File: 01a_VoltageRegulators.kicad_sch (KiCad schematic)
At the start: 34 parts, among them U5 TPS54331, U6 TPS56637RPAR, U7 TLV75733PDBV

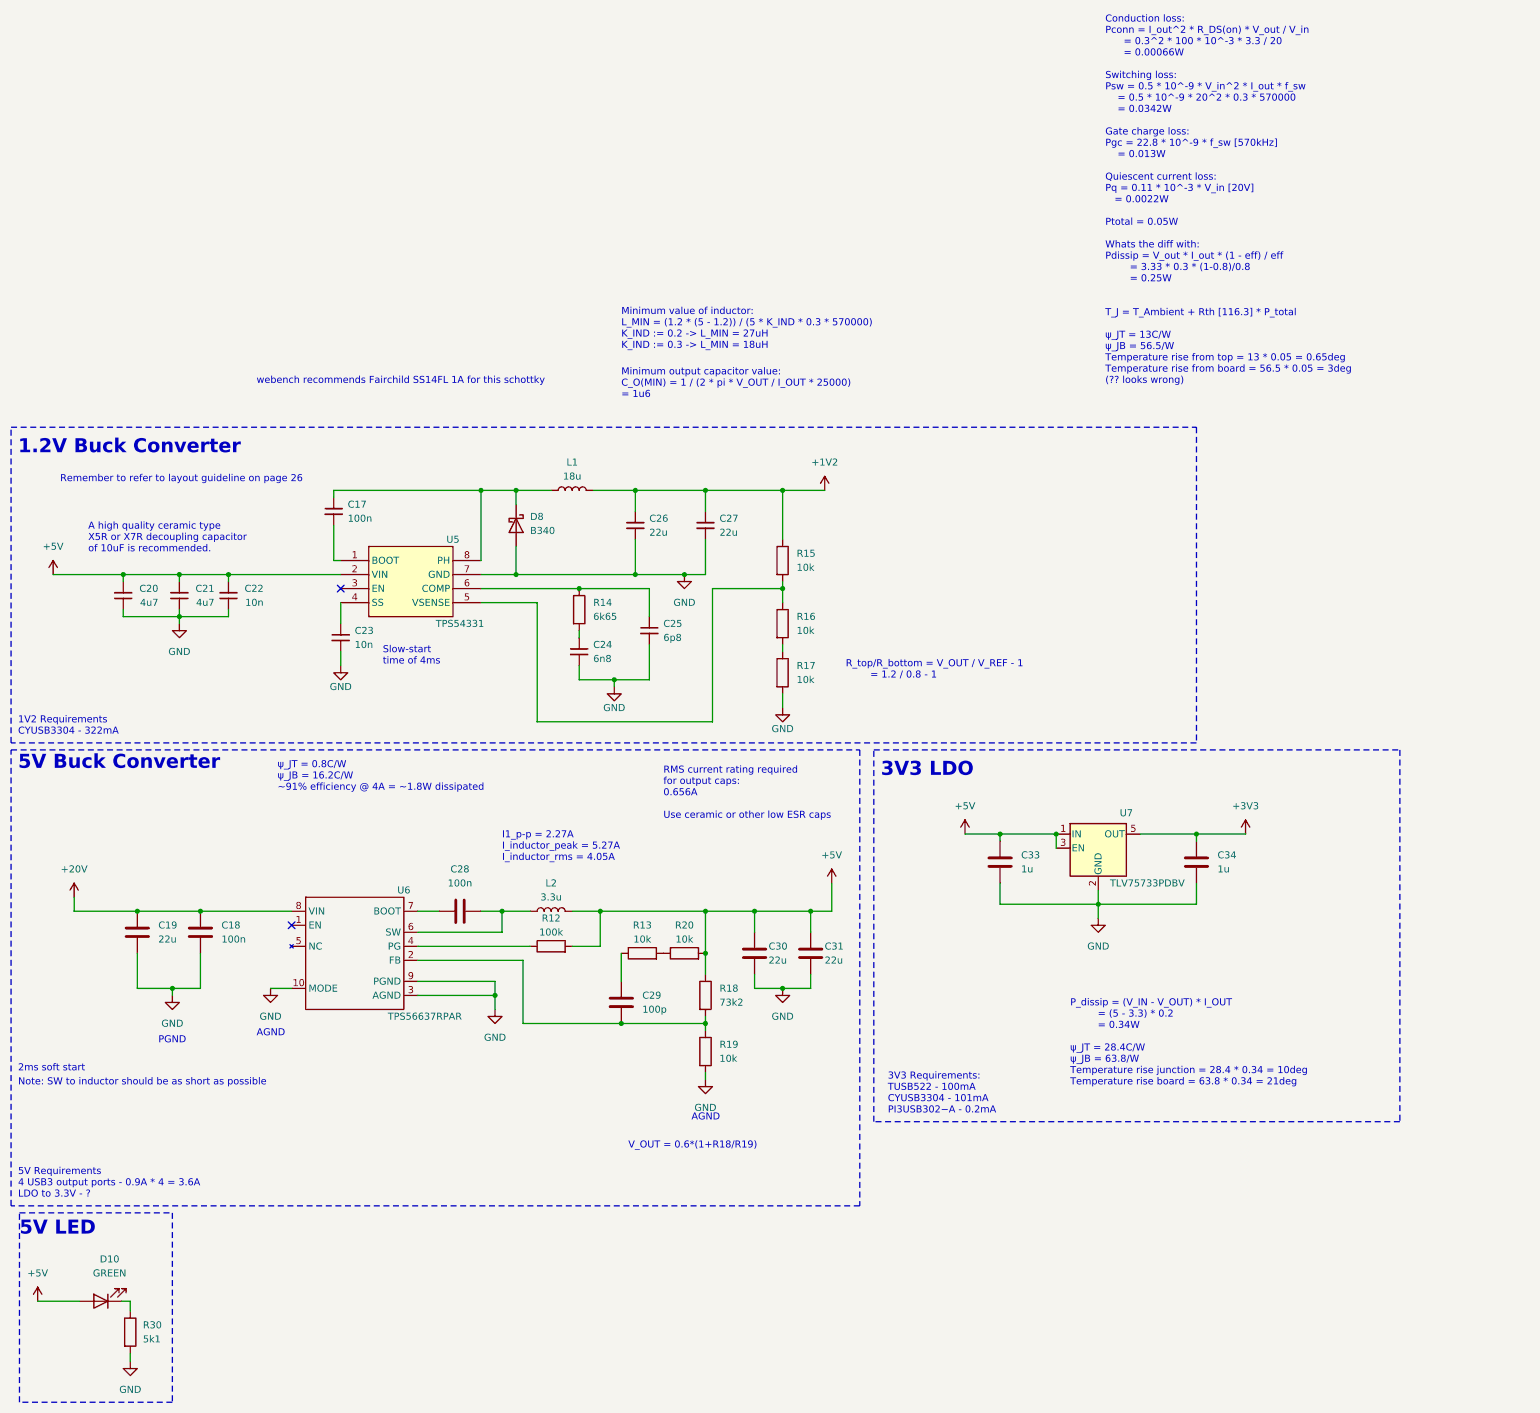
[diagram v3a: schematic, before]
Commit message: finish up schematics and ERC
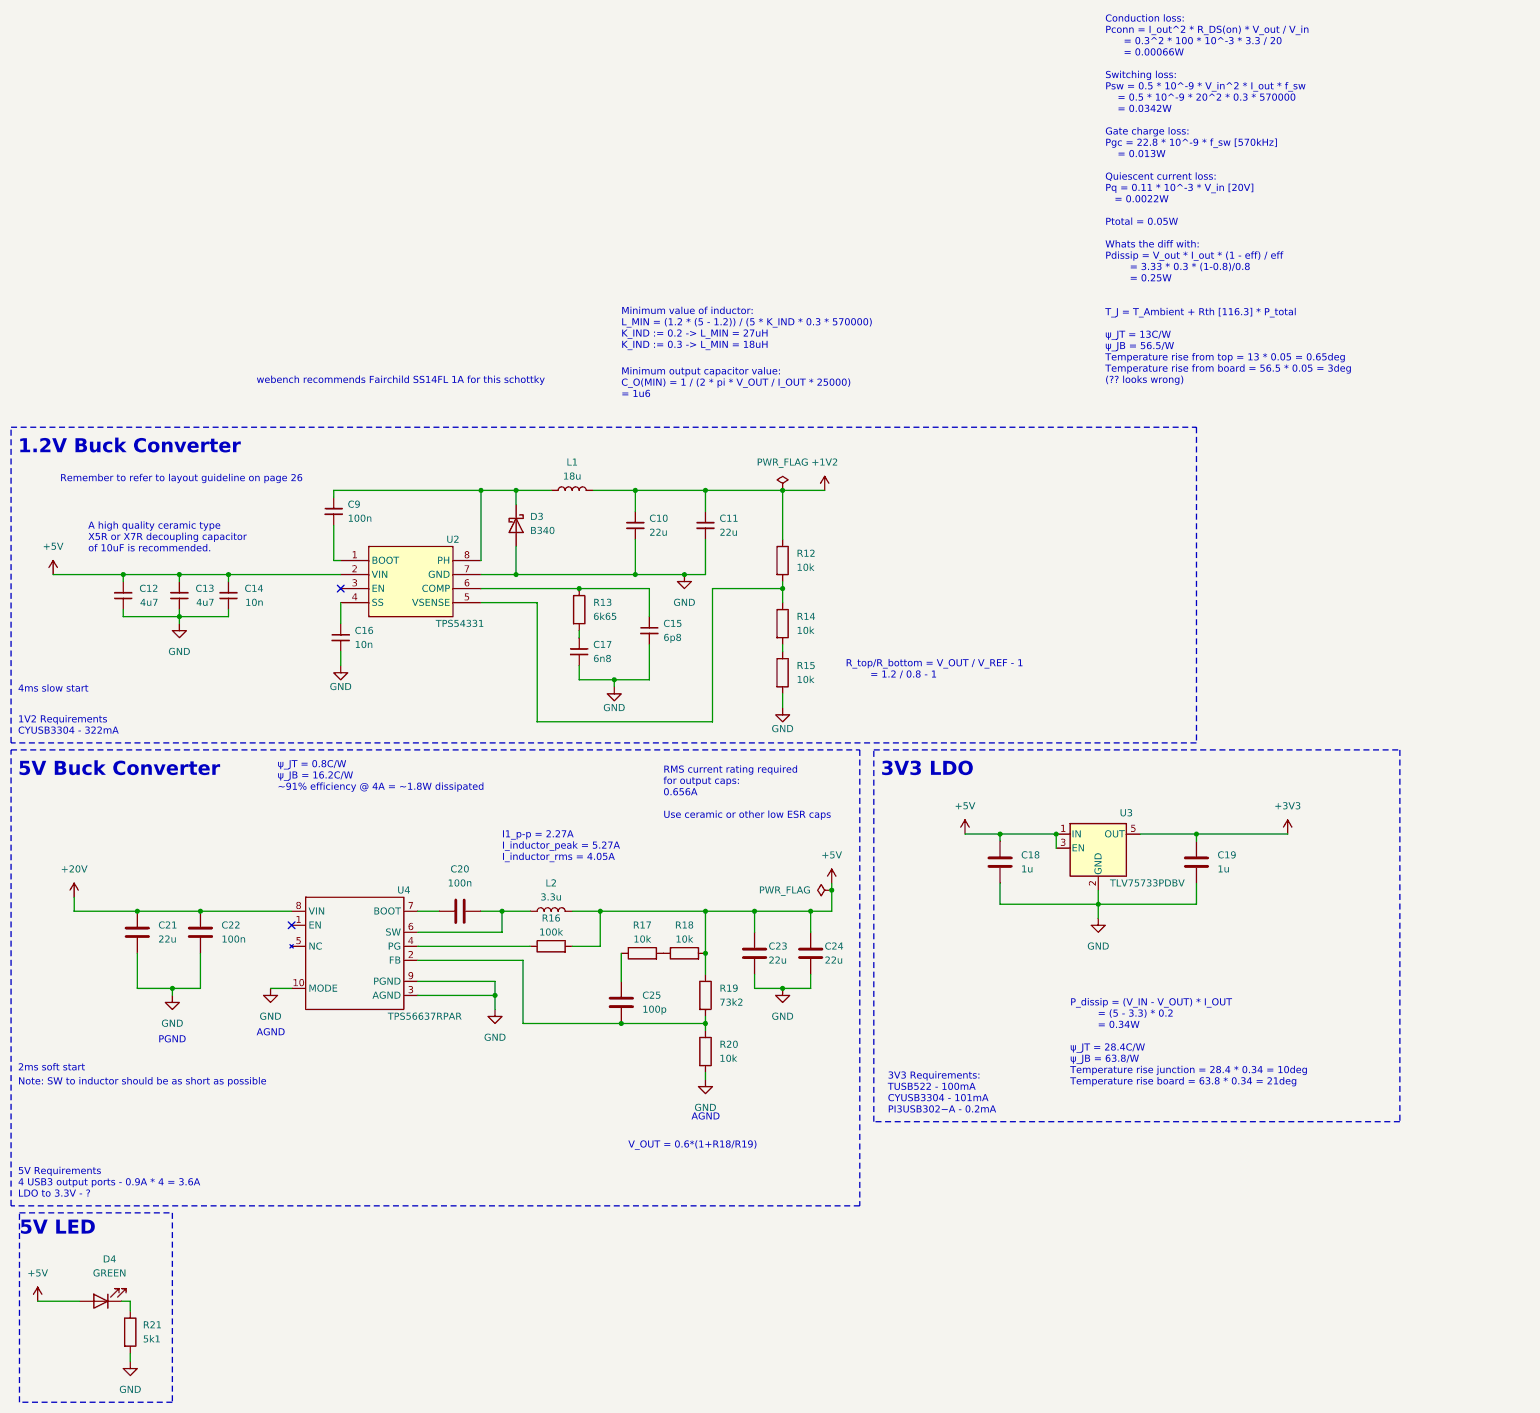
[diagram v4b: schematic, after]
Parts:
- renumbered C26 to C10, C27 to C11, C20 to C12, C21 to C13, C22 to C14, C25 to C15, C23 to C16, C24 to C17, C33 to C18, C34 to C19, C28 to C20, C19 to C21, C18 to C22, C30 to C23, C31 to C24, C29 to C25, C17 to C9, D8 to D3, D10 to D4, R15 to R12, R14 to R13, R16 to R14, R17 to R15, R12 to R16, R13 to R17, R20 to R18, R18 to R19, R19 to R20, R30 to R21, U5 to U2, U7 to U3, U6 to U4
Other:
- note added: "4ms slow start"
- note removed: "Slow-start time of 4ms"

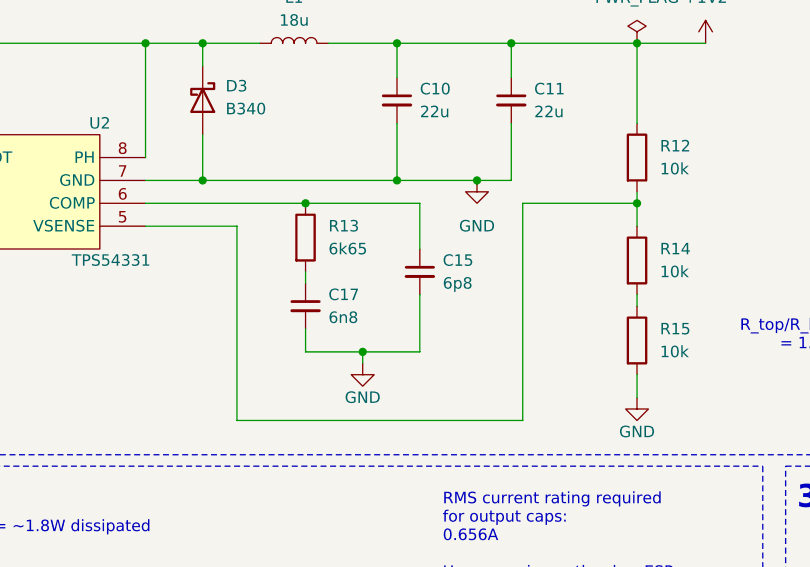
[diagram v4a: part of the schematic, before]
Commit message: finish setting footprints
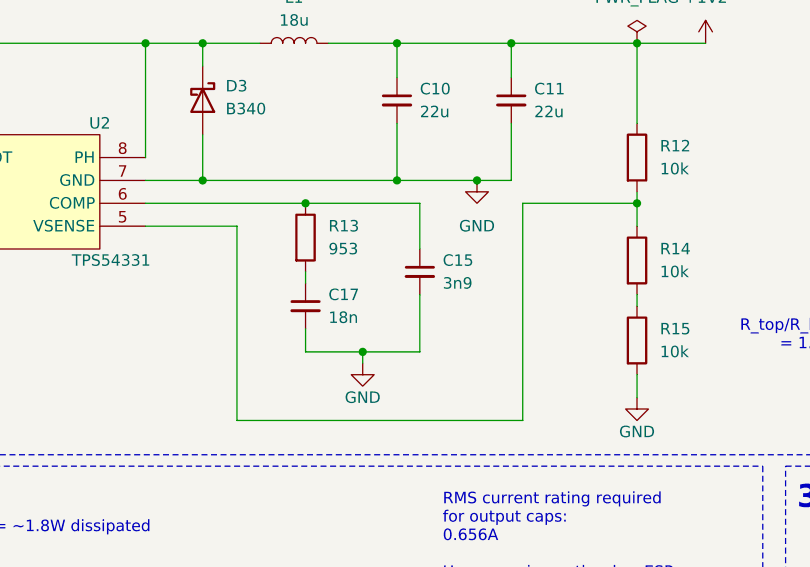
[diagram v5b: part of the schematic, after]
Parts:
- C10, C11, C12, C13, C14, C16, C18, C19, C20, C21, C22, C23, C24, C25, C9: footprint (none) -> Capacitor_SMD:C_0603_1608Metric
- C15: value 6p8 -> 3n9; footprint (none) -> Capacitor_SMD:C_0603_1608Metric
- C17: value 6n8 -> 18n; footprint (none) -> Capacitor_SMD:C_0603_1608Metric
- L1: footprint (none) -> CakeUSB:FNR6045Sx
- L2: footprint (none) -> CakeUSB:FXL0630x
- R12, R14, R15, R16, R17, R18, R20: footprint (none) -> Resistor_SMD:R_0603_1608Metric
- R13: value 6k65 -> 953; footprint (none) -> Resistor_SMD:R_0603_1608Metric
- R19: footprint (none) -> Resistor_SMD:R_0402_1005Metric
- U2: footprint (none) -> CakeUSB:TPS54331DR
- U4: footprint (none) -> CakeUSB:TPS56637RPAR
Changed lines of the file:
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@@
       (effects (font (size 1.27 1.27)) (justify left))
     )
-    (property "Footprint" "" (at 72.39 50.8 0)
+    (property "Footprint" "Capacitor_SMD:C_0603_1608Metric" (at 72.39 50.8 0)
       (effects (font (size 1.27 1.27)) hide)
     )
@@
       (effects (font (size 1.27 1.27)) (justify left))
     )
-    (property "Footprint" "" (at 138.43 30.48 0)
+    (property "Footprint" "Capacitor_SMD:C_0603_1608Metric" (at 138.43 30.48 0)
       (effects (font (size 1.27 1.27)) hide)
     )
@@
       (effects (font (size 1.27 1.27)) (justify left))
     )
-    (property "Footprint" "" (at 136.652 125.73 90)
+    (property "Footprint" "Resistor_SMD:R_0603_1608Metric" (at 136.652 125.73 90)
       (effects (font (size 1.27 1.27)) hide)
     )
@@
       (effects (font (size 1.27 1.27)) (justify left))
     )
-    (property "Footprint" "" (at 71.12 27.94 0)
+    (property "Footprint" "Capacitor_SMD:C_0603_1608Metric" (at 71.12 27.94 0)
       (effects (font (size 1.27 1.27)) hide)
     )
@@
       (effects (font (size 1.27 1.27)))
     )
-    (property "Footprint" "" (at 134.62 109.728 90)
+    (property "Footprint" "Resistor_SMD:R_0603_1608Metric" (at 134.62 109.728 90)
       (effects (font (size 1.27 1.27)) hide)
     )
@@
       (effects (font (size 1.27 1.27)) (justify left))
     )
-    (property "Footprint" "" (at 47.9552 107.95 0)
+    (property "Footprint" "Capacitor_SMD:C_0603_1608Metric" (at 47.9552 107.95 0)
       (effects (font (size 1.27 1.27)) hide)
     )
@@
       (effects (font (size 1.27 1.27)))
     )
-    (property "Footprint" "" (at 110.49 108.458 90)
+    (property "Footprint" "Resistor_SMD:R_0603_1608Metric" (at 110.49 108.458 90)
       (effects (font (size 1.27 1.27)) hide)
     )
@@
       (effects (font (size 1.27 1.27)) (justify left))
     )
-    (property "Footprint" "" (at 192.7352 95.25 0)
+    (property "Footprint" "Capacitor_SMD:C_0603_1608Metric" (at 192.7352 95.25 0)
       (effects (font (size 1.27 1.27)) hide)
     )
@@
       (effects (font (size 1.27 1.27)))
     )
-    (property "Footprint" "" (at 97.79 99.3648 0)
+    (property "Footprint" "Capacitor_SMD:C_0603_1608Metric" (at 97.79 99.3648 0)
       (effects (font (size 1.27 1.27)) hide)
     )
@@
       (effects (font (size 1.27 1.27)) (justify left))
     )
-    (property "Footprint" "" (at 228.2952 95.25 0)
+    (property "Footprint" "Capacitor_SMD:C_0603_1608Metric" (at 228.2952 95.25 0)
       (effects (font (size 1.27 1.27)) hide)
     )
@@
       (effects (font (size 1.27 1.27)) (justify left))
     )
-    (property "Footprint" "" (at 150.622 48.26 90)
+    (property "Footprint" "Resistor_SMD:R_0603_1608Metric" (at 150.622 48.26 90)
       (effects (font (size 1.27 1.27)) hide)
     )
@@
       (effects (font (size 1.27 1.27)) (justify left))
     )
-    (property "Footprint" "" (at 43.18 43.18 0)
+    (property "Footprint" "Capacitor_SMD:C_0603_1608Metric" (at 43.18 43.18 0)
       (effects (font (size 1.27 1.27)) hide)
     )
@@
       (effects (font (size 1.27 1.27)) (justify left))
     )
-    (property "Footprint" "" (at 125.73 30.48 0)
+    (property "Footprint" "Capacitor_SMD:C_0603_1608Metric" (at 125.73 30.48 0)
       (effects (font (size 1.27 1.27)) hide)
     )
@@
       (effects (font (size 1.27 1.27)) (justify left))
     )
-    (property "Value" "6p8" (at 130.81 50.8063 0)
-      (effects (font (size 1.27 1.27)) (justify left))
-    )
-    (property "Footprint" "" (at 128.27 49.53 0)
+    (property "Value" "3n9" (at 130.81 50.8063 0)
+      (effects (font (size 1.27 1.27)) (justify left))
+    )
+    (property "Footprint" "Capacitor_SMD:C_0603_1608Metric" (at 128.27 49.53 0)
       (effects (font (size 1.27 1.27)) hide)
     )
@@
       (effects (font (size 1.27 1.27)) (justify left))
     )
-    (property "Value" "6n8" (at 118.11 54.6163 0)
-      (effects (font (size 1.27 1.27)) (justify left))
-    )
-    (property "Footprint" "" (at 115.57 53.34 0)
+    (property "Value" "18n" (at 118.11 54.6163 0)
+      (effects (font (size 1.27 1.27)) (justify left))
+    )
+    (property "Footprint" "Capacitor_SMD:C_0603_1608Metric" (at 115.57 53.34 0)
       (effects (font (size 1.27 1.27)) hide)
     )
@@
       (effects (font (size 1.27 1.27)))
     )
-    (property "Footprint" "" (at 127 109.728 90)
+    (property "Footprint" "Resistor_SMD:R_0603_1608Metric" (at 127 109.728 90)
       (effects (font (size 1.27 1.27)) hide)
     )
@@
       (effects (font (size 1.27 1.27)))
     )
-    (property "Footprint" "" (at 85.09 40.64 0)
+    (property "Footprint" "CakeUSB:TPS54331DR" (at 85.09 40.64 0)
       (effects (font (size 1.27 1.27)) hide)
     )
@@
       (effects (font (size 1.27 1.27)) (justify left))
     )
-    (property "Footprint" "" (at 124.1552 120.65 0)
+    (property "Footprint" "Capacitor_SMD:C_0603_1608Metric" (at 124.1552 120.65 0)
       (effects (font (size 1.27 1.27)) hide)
     )
@@
       (effects (font (size 1.27 1.27)) (justify left))
     )
-    (property "Footprint" "" (at 158.4452 111.76 0)
+    (property "Footprint" "Capacitor_SMD:C_0603_1608Metric" (at 158.4452 111.76 0)
       (effects (font (size 1.27 1.27)) hide)
     )
@@
       (effects (font (size 1.27 1.27)) (justify left))
     )
-    (property "Footprint" "" (at 150.622 57.15 90)
+    (property "Footprint" "Resistor_SMD:R_0603_1608Metric" (at 150.622 57.15 90)
       (effects (font (size 1.27 1.27)) hide)
     )
@@
       (effects (font (size 1.27 1.27)) (justify left))
     )
-    (property "Footprint" "" (at 150.622 36.83 90)
+    (property "Footprint" "Resistor_SMD:R_0603_1608Metric" (at 150.622 36.83 90)
       (effects (font (size 1.27 1.27)) hide)
     )
@@
       (effects (font (size 1.27 1.27)) (justify left))
     )
-    (property "Footprint" "" (at 36.5252 107.95 0)
+    (property "Footprint" "Capacitor_SMD:C_0603_1608Metric" (at 36.5252 107.95 0)
       (effects (font (size 1.27 1.27)) hide)
     )
@@
       (effects (font (size 1.27 1.27)) (justify left))
     )
-    (property "Value" "6k65" (at 118.11 46.99 0)
-      (effects (font (size 1.27 1.27)) (justify left))
-    )
-    (property "Footprint" "" (at 113.792 45.72 90)
+    (property "Value" "953" (at 118.11 46.99 0)
+      (effects (font (size 1.27 1.27)) (justify left))
+    )
+    (property "Footprint" "Resistor_SMD:R_0603_1608Metric" (at 113.792 45.72 90)
       (effects (font (size 1.27 1.27)) hide)
     )
@@
       (effects (font (size 1.27 1.27)))
     )
-    (property "Footprint" "" (at 74.93 107.95 0)
+    (property "Footprint" "CakeUSB:TPS56637RPAR" (at 74.93 107.95 0)
       (effects (font (size 1.27 1.27)) hide)
     )
@@
       (effects (font (size 1.27 1.27)) (justify left))
     )
-    (property "Footprint" "" (at 148.2852 111.76 0)
+    (property "Footprint" "Capacitor_SMD:C_0603_1608Metric" (at 148.2852 111.76 0)
       (effects (font (size 1.27 1.27)) hide)
     )
@@
       (effects (font (size 1.27 1.27)) (justify left))
     )
-    (property "Footprint" "" (at 136.652 115.57 90)
+    (property "Footprint" "Resistor_SMD:R_0402_1005Metric" (at 136.652 115.57 90)
       (effects (font (size 1.27 1.27)) hide)
     )
@@
       (effects (font (size 1.27 1.27)) (justify left))
     )
-    (property "Footprint" "" (at 52.07 43.18 0)
+    (property "Footprint" "Capacitor_SMD:C_0603_1608Metric" (at 52.07 43.18 0)
       (effects (font (size 1.27 1.27)) hide)
     )
@@
       (effects (font (size 1.27 1.27)))
     )
-    (property "Footprint" "" (at 114.3 24.13 0)
+    (property "Footprint" "CakeUSB:FNR6045Sx" (at 114.3 24.13 0)
       (effects (font (size 1.27 1.27)) hide)
     )
@@
       (effects (font (size 1.27 1.27)) (justify left))
     )
-    (property "Footprint" "" (at 33.02 43.18 0)
+    (property "Footprint" "Capacitor_SMD:C_0603_1608Metric" (at 33.02 43.18 0)
       (effects (font (size 1.27 1.27)) hide)
     )
@@
       (effects (font (size 1.27 1.27)))
     )
-    (property "Footprint" "" (at 110.49 100.33 0)
-      (effects (font (size 1.27 1.27)) hide)
-    )
+    (property "Footprint" "CakeUSB:FXL0630x" (at 110.49 100.33 0)
+      (effects (font (size 1.27 1.27)) hide)
+    )
